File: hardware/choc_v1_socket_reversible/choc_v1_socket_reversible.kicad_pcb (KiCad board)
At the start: 2 copper layers, 143.8 x 104.4 mm, 76 parts, among them SW00 SW_Push, SW01 SW_Push, SW02 SW_Push, SW03 SW_Push, SW04 SW_Push, SW05 SW_Push, SW10 SW_Push, SW11 SW_Push, SW12 SW_Push, SW13 SW_Push, SW14 SW_Push, SW15 SW_Push, SW20 SW_Push, SW21 SW_Push, SW22 SW_Push, SW23 SW_Push, SW24 SW_Push, SW25 SW_Push, SW30 SW_Push, SW31 SW_Push, SW32 SW_Push, SW33 SW_Push, SW34 SW_Push, SW35 SW_Push, SW36 SW_Push, SW37 SW_Push, U1 CH582

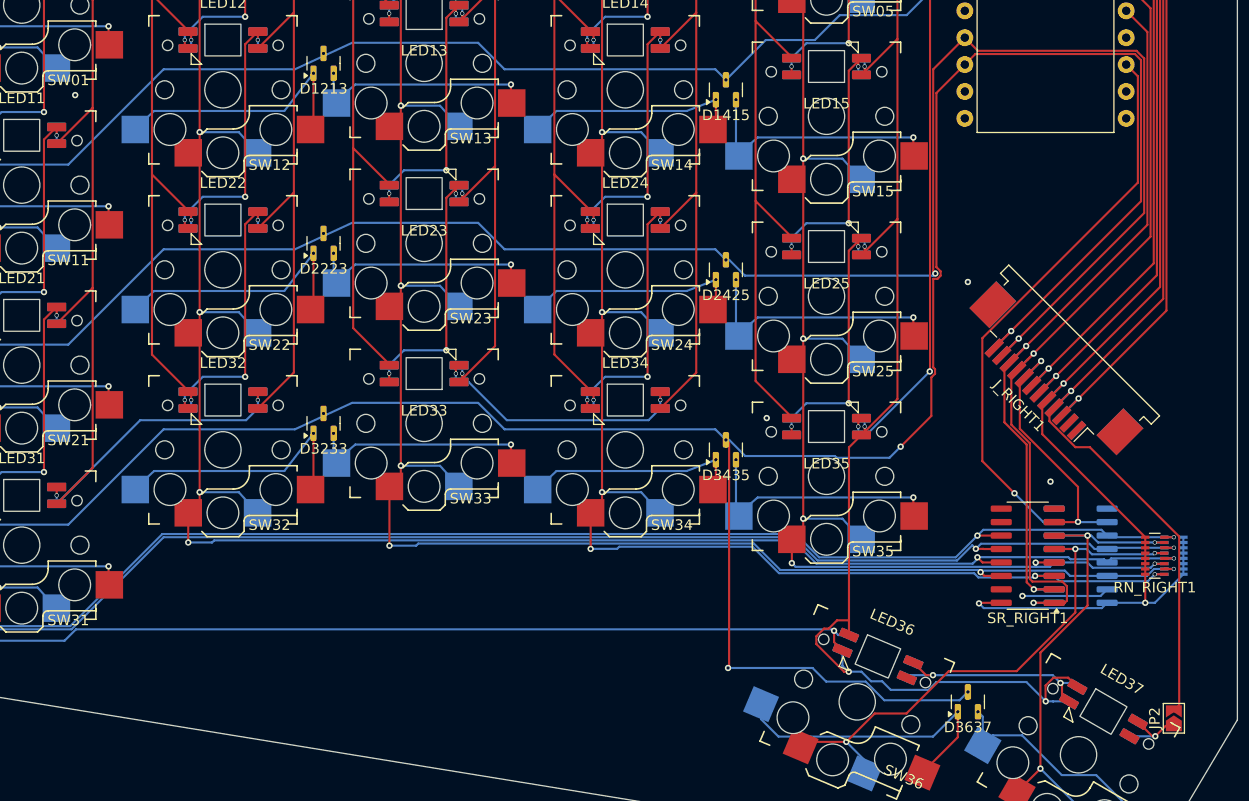
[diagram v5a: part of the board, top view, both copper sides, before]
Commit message: Improved copper pour
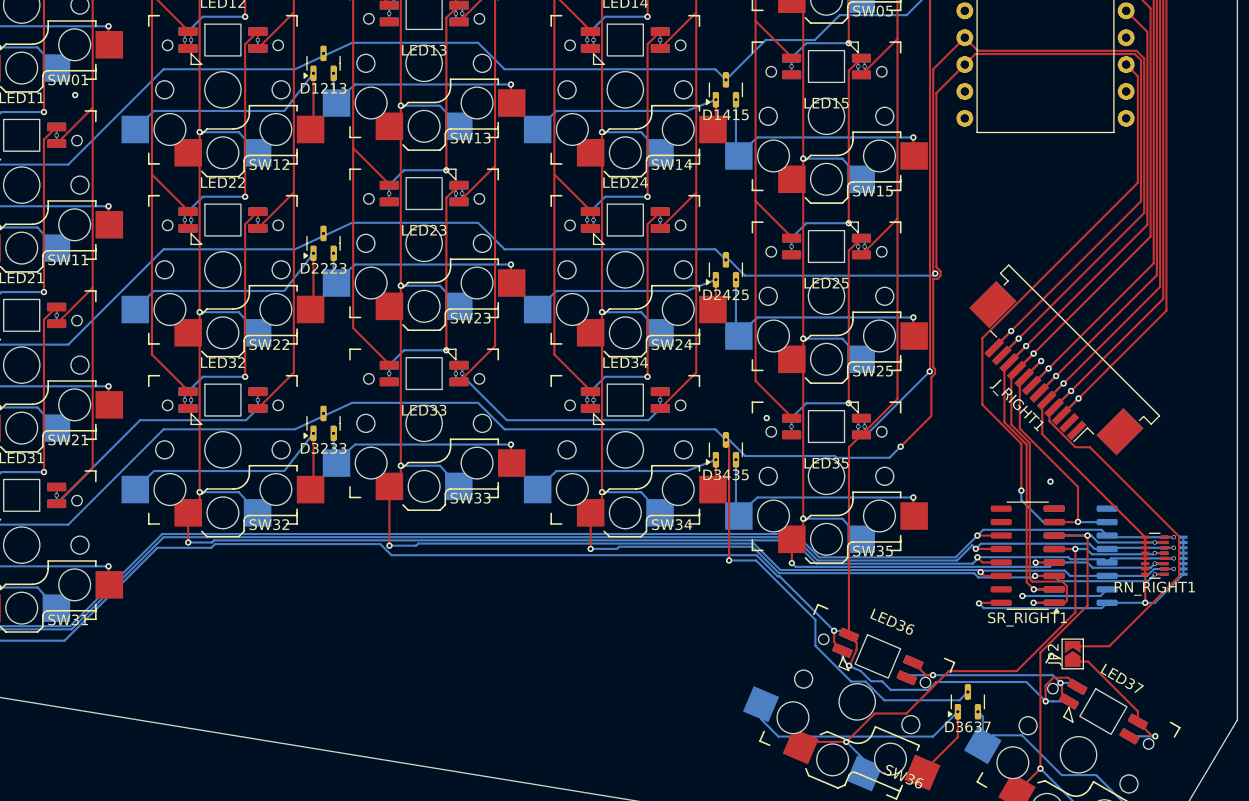
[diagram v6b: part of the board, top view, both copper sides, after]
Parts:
- moved JP2 11.3 mm to (178.2, 121.3)
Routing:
- net Net-(JP2-A): track 6.80 -> 13.7 mm
- net Net-(LED30-DIN): track 113.7 -> 120.4 mm
- net +5V: track 682.1 -> 676.5 mm
- net ROW3: track 237.5 -> 232.9 mm
- net GND: vias 7 -> 6

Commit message: Generated gerber
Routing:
- net COL0: track 211.8 -> 216.8 mm
- net ROW3: track 232.9 -> 236.6 mm
- net ROW2: track 179.8 -> 182.3 mm
- net COL1: track 201.5 -> 203.9 mm
- net Net-(LED30-DIN): track 120.4 -> 122.5 mm
- net Net-(LED35-DIN): track 59.9 -> 62.0 mm
- net COL3: track 162.2 -> 160.6 mm
- net ROW0: track 172.2 -> 171.1 mm
- net LED_R: track 96.8 -> 97.6 mm
- net SCK0: track 67.7 -> 68.5 mm
- net +3V3: track 104.1 -> 103.5 mm
- net COL2: track 178.7 -> 179.3 mm
- net DS: track 25.0 -> 25.5 mm
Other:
- board size 143.8 x 104.4 mm -> 143.8 x 103.6 mm

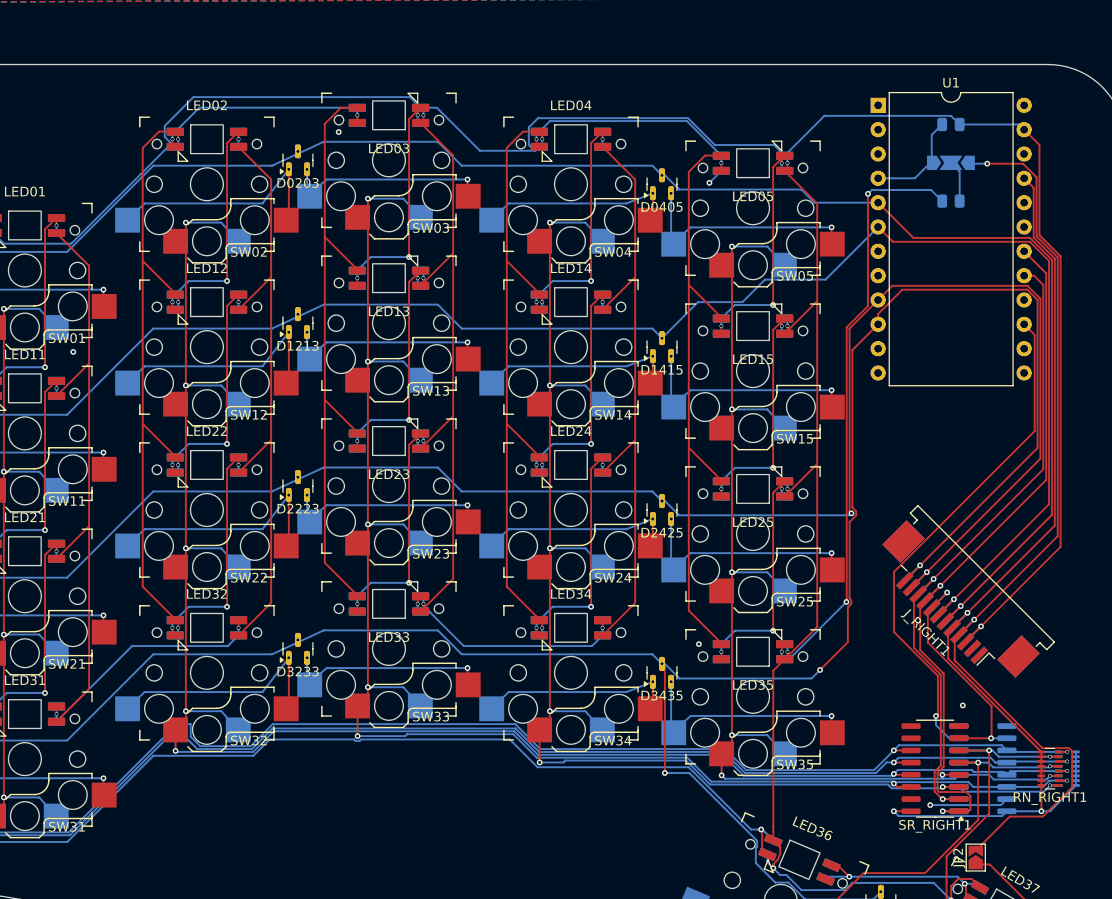
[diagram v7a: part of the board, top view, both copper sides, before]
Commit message: Added mounting hole and antenna cutout
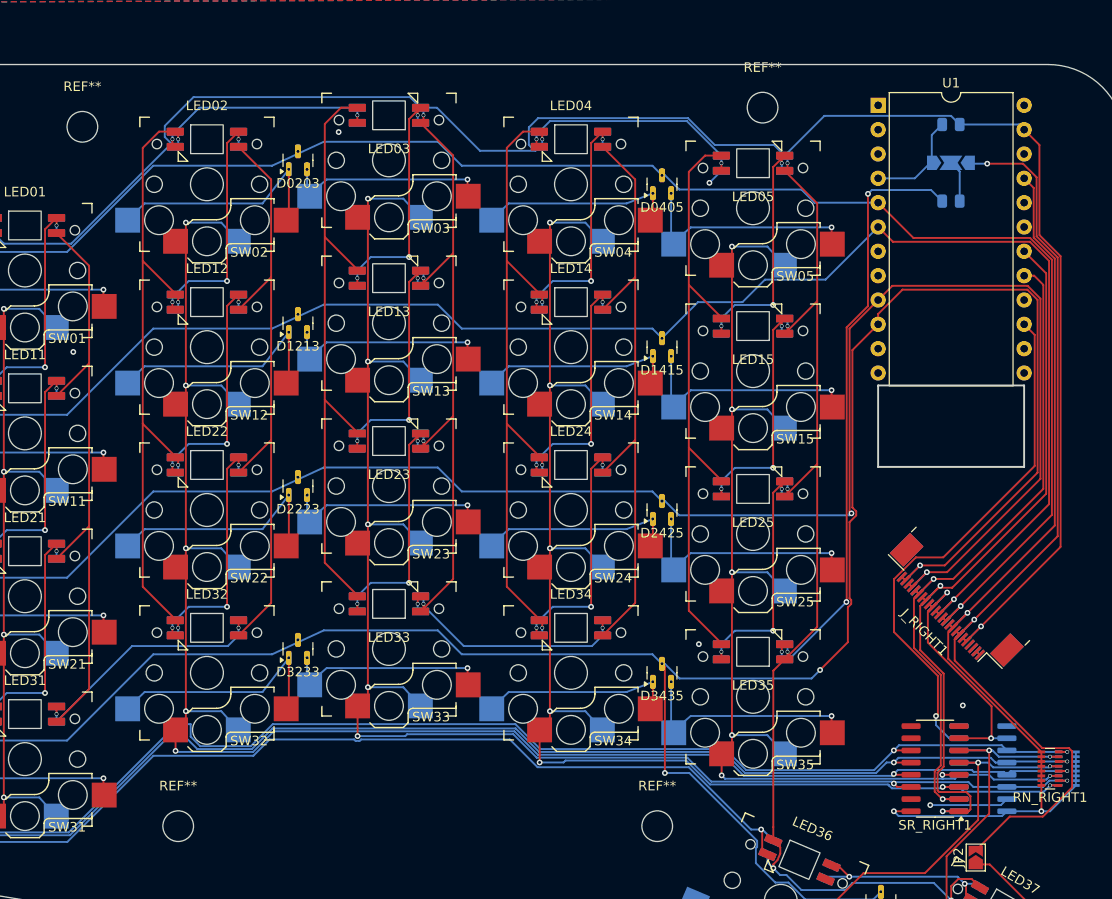
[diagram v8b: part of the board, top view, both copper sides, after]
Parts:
- added REF**: MountingHole_3.2mm_M3, MountingHole:MountingHole_3.2mm_M3, F.Cu at (145.0, 118.0)
- added REF**: MountingHole_3.2mm_M3, MountingHole:MountingHole_3.2mm_M3, F.Cu at (85.0, 45.0)
- added REF**: MountingHole_3.2mm_M3, MountingHole:MountingHole_3.2mm_M3, F.Cu at (156.0, 43.0)
- added REF**: MountingHole_3.2mm_M3, MountingHole:MountingHole_3.2mm_M3, F.Cu at (95.0, 118.0)
- J_LEFT1, J_RIGHT1: value Conn_01x12_MountingPin -> Conn_02x12_Odd_Even_MountingPin; footprint Connector_FFC-FPC:TE_1-84952-2_1x12-1MP_P1.0mm_Horizontal -> Connector_FFC-FPC:Jushuo_AFC07-S24FCA-00_1x24-1MP_P0.50_Horizontal
- moved J_RIGHT1 0.27 mm to (175.7, 94.9)
- moved J_LEFT1 0.27 mm to (175.7, 94.9)
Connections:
- J_LEFT1 pad 10: +5V -> DS
- J_LEFT1 pad 11: unconnected-(J_LEFT1-Pin_11-Pad11) -> ROW1
- J_LEFT1 pad 12: GND -> ROW1
- J_LEFT1 pad 2: ROW2 -> ROW3
- J_LEFT1 pad 3: SCK0 -> ROW2
- J_LEFT1 pad 4: SCS -> ROW2
- J_LEFT1 pad 5: DS -> SCK0
- J_LEFT1 pad 6: ROW1 -> SCK0
- J_LEFT1 pad 7: ROW0 -> SCS
- J_LEFT1 pad 8: +3V3 -> SCS
- J_LEFT1 pad 9: LED_R -> DS
- J_RIGHT1 pad 10: SCK0 -> +3V3
- J_RIGHT1 pad 11: ROW2 -> ROW0
- J_RIGHT1 pad 12: ROW3 -> ROW0
- J_RIGHT1 pad 2: unconnected-(J_RIGHT1-Pin_2-Pad2) -> GND
- J_RIGHT1 pad 3: +5V -> unconnected-(J_RIGHT1-Pin_3-Pad3)
- J_RIGHT1 pad 4: LED_R -> unconnected-(J_RIGHT1-Pin_4-Pad4)
- J_RIGHT1 pad 5: +3V3 -> +5V
- J_RIGHT1 pad 6: ROW0 -> +5V
- J_RIGHT1 pad 7: ROW1 -> LED_R
- J_RIGHT1 pad 8: DS -> LED_R
- J_RIGHT1 pad 9: SCS -> +3V3
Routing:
- net SCK0: track 68.5 -> 71.4 mm
- net SCS: track 76.0 -> 78.7 mm
- net ROW3: track 236.6 -> 239.2 mm
- net ROW2: track 182.3 -> 184.5 mm
- net LED_R: track 97.6 -> 99.3 mm
- net MISO: track 53.3 -> 55.0 mm
- net GND: track 393.3 -> 394.3 mm
- net +5V: track 676.6 -> 677.6 mm
- net DS: track 25.5 -> 26.5 mm
- net +3V3: track 103.5 -> 104.5 mm
- net ROW1: track 172.8 -> 173.8 mm
- net ROW0: track 171.1 -> 172.1 mm
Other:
- outline, holes or cut-outs redrawn
